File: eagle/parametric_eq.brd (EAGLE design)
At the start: 100 x 80 mm, 42 parts, among them IC1 TL072P, IC2 TL072P

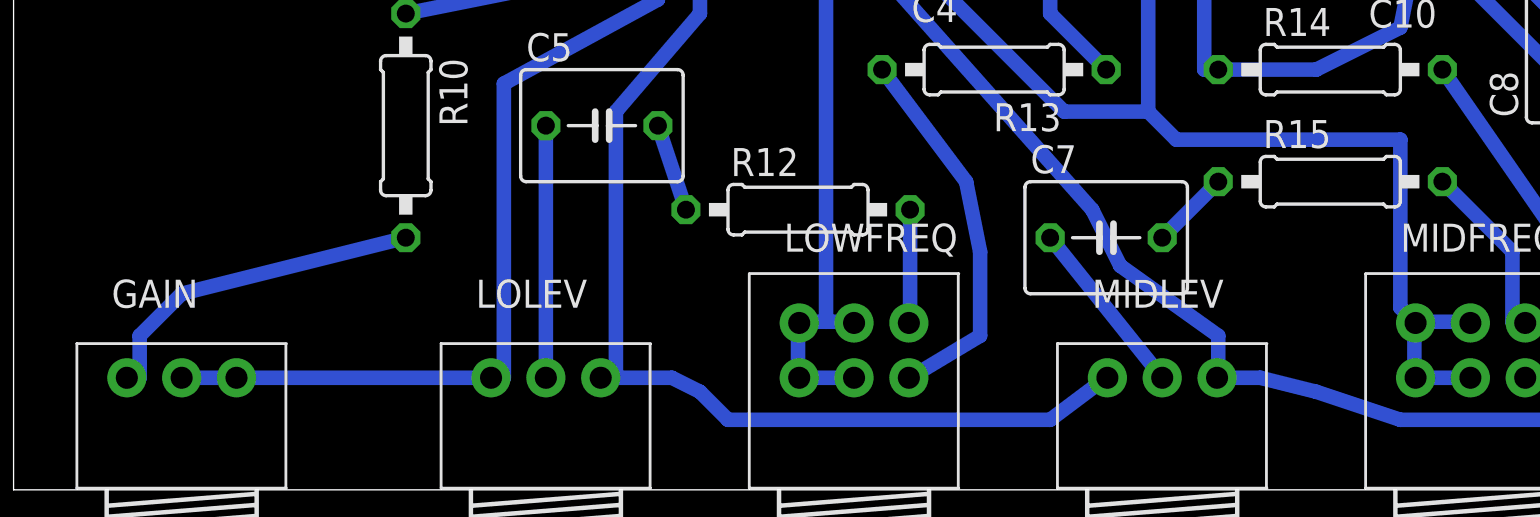
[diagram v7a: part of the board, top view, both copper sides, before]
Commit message: improved traces
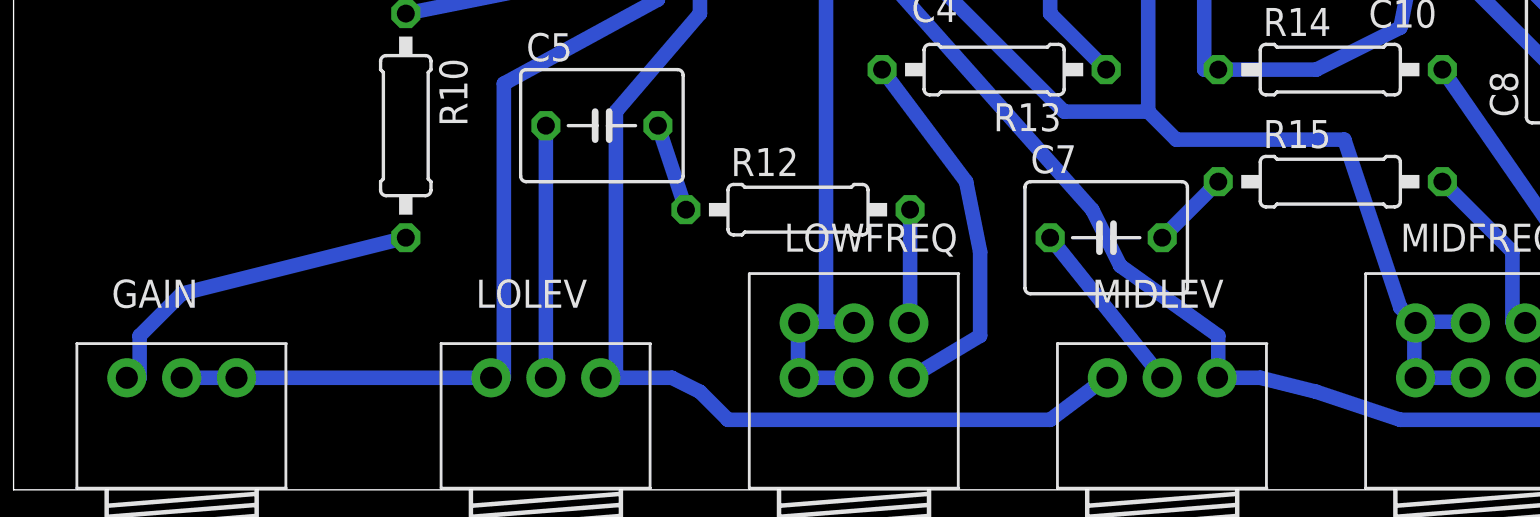
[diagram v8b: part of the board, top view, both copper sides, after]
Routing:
- net N$27: track 76.9 -> 74.7 mm
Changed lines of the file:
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@@
 <contactref element="R10" pad="2"/>
 <contactref element="GAIN" pad="1"/>
-<wire x1="5.715" y1="5.715" x2="5.715" y2="6.985" width="0.6604" layer="16"/>
+<wire x1="5.715" y1="5.08" x2="5.715" y2="6.985" width="0.6604" layer="16"/>
 <wire x1="5.715" y1="6.985" x2="7.62" y2="8.89" width="0.6604" layer="16"/>
 <wire x1="7.62" y1="8.89" x2="17.78" y2="11.43" width="0.6604" layer="16"/>
-<wire x1="5.715" y1="5.08" x2="5.715" y2="5.715" width="0.6604" layer="16"/>
 <wire x1="5.715" y1="5.08" x2="5.1346" y2="5.08" width="0.6604" layer="16"/>
 </signal>
@@
 <wire x1="51.435" y1="17.145" x2="51.435" y2="26.035" width="0.6604" layer="16"/>
 <wire x1="52.705" y1="15.875" x2="51.435" y2="17.145" width="0.6604" layer="16"/>
-<wire x1="62.865" y1="15.875" x2="52.705" y2="15.875" width="0.6604" layer="16"/>
-<wire x1="62.865" y1="8.255" x2="62.865" y2="15.875" width="0.6604" layer="16"/>
+<wire x1="60.325" y1="15.875" x2="52.705" y2="15.875" width="0.6604" layer="16"/>
+<wire x1="62.865" y1="8.255" x2="60.325" y2="15.875" width="0.6604" layer="16"/>
 <wire x1="63.5546" y1="7.5654" x2="62.865" y2="8.255" width="0.6604" layer="16"/>
 <wire x1="45.72" y1="30.48" x2="60.96" y2="30.48" width="0.6604" layer="16"/>
